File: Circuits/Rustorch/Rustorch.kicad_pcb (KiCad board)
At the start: 4 copper layers, 95 x 72 mm, 57 parts, among them CN1 USB_C_Receptacle_USB2.0_16P, CN2 OLED_128x64_IIC, Q1 2SC1815, Q2 2SC1815, Q3 2SC1815, Q4 2SC1815, SW1 ToggleSW 3P, SW2 RESET, SW3 SW_BOOT, SW4 SW_UP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

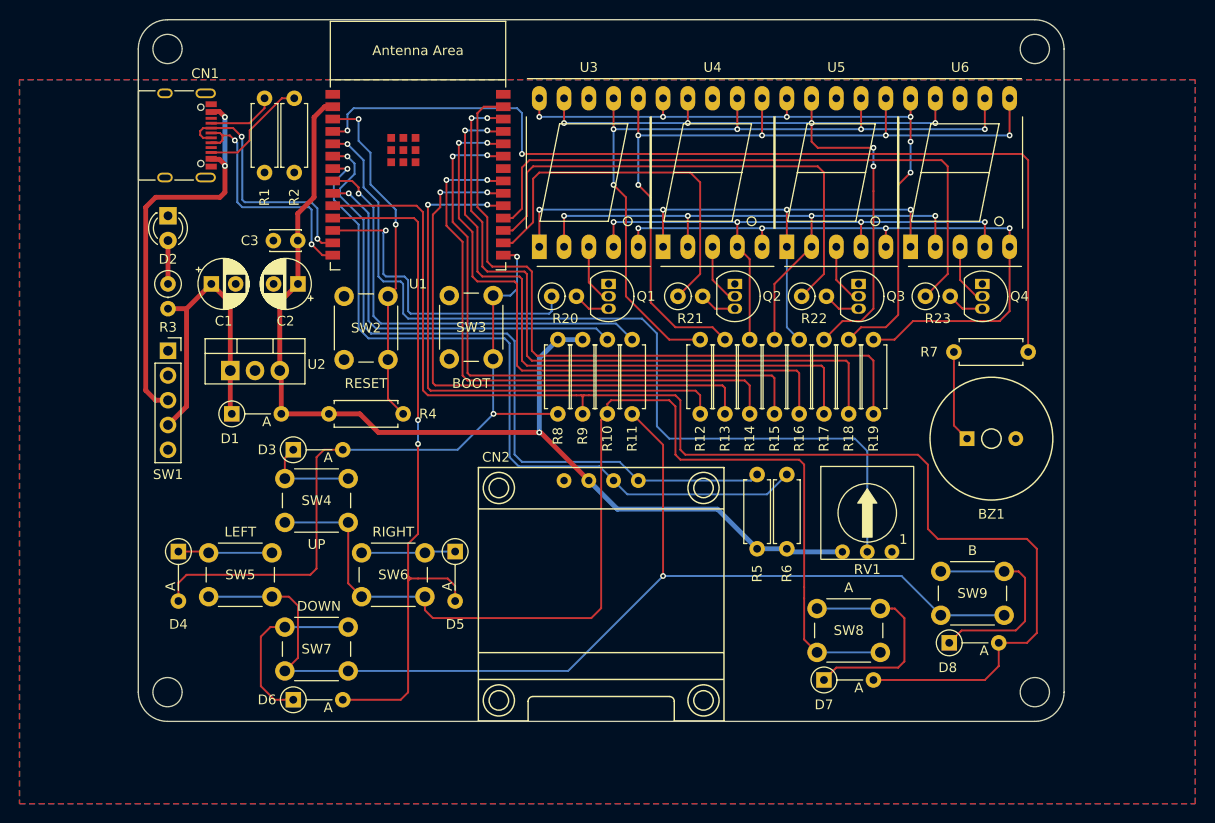
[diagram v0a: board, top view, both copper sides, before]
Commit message: (Rustorch) 配線作業 (配線を2層に削減可能な状態へ修正)
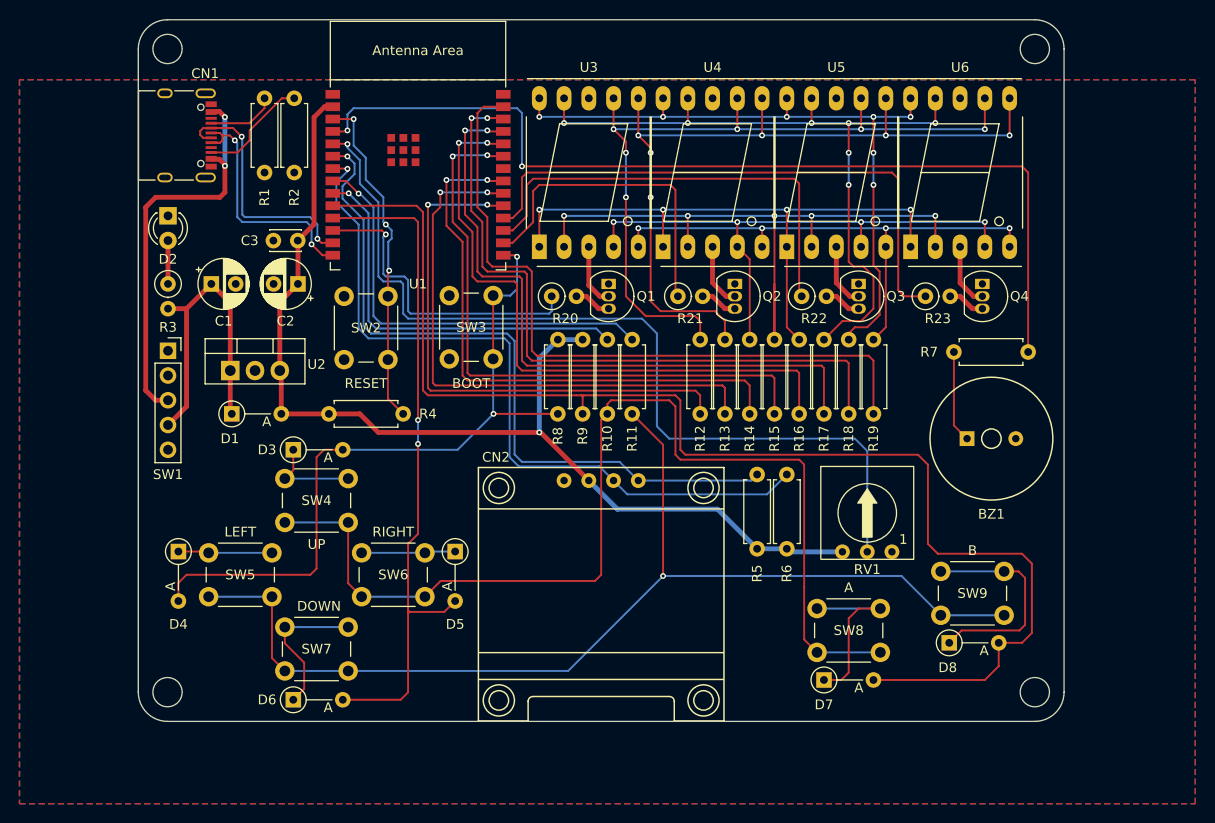
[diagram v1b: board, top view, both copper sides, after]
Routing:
- net /DP: track 67.5 -> 55.8 mm
- net /D: track 61.9 -> 69.2 mm, vias 4 -> 5
- net 7SEG_DIGIT3: track 52.2 -> 46.3 mm
- net 7SEG_DIGIT2: track 38.9 -> 33.2 mm
- net 7SEG_DIGIT4: track 65.1 -> 59.7 mm
- net Net-(R10-Pad1): track 115.0 -> 110.3 mm
- net /F: track 79.7 -> 75.4 mm, vias 6 -> 7
- net Net-(D7-K): track 22.9 -> 18.6 mm
- net Net-(D6-K): track 18.4 -> 15.2 mm
- net Net-(R11-Pad1): track 114.3 -> 112.1 mm
- net /A: track 77.9 -> 79.8 mm, vias 5 -> 6
- net /G: track 72.7 -> 70.9 mm, vias 6 -> 7
- net KEY_IN2: track 72.0 -> 70.4 mm
- net /B: track 80.2 -> 81.3 mm, vias 5 -> 6
- net KEY_IN3_IO8: track 135.3 -> 134.3 mm
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
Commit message: (Rustorch) 配線作業 (配線を2層化)
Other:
- copper layers 4 -> 2
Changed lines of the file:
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@@
 	(layers
 		(0 "F.Cu" signal)
-		(1 "In1.Cu" signal)
-		(2 "In2.Cu" signal)
 		(31 "B.Cu" signal)
 		(32 "B.Adhes" user "B.Adhesive")
@@
 			)
 			(layer "dielectric 1"
-				(type "prepreg")
-				(thickness 0.1)
-				(material "FR4")
-				(epsilon_r 4.5)
-				(loss_tangent 0.02)
-			)
-			(layer "In1.Cu"
-				(type "copper")
-				(thickness 0.035)
-			)
-			(layer "dielectric 2"
 				(type "core")
-				(thickness 1.24)
-				(material "FR4")
-				(epsilon_r 4.5)
-				(loss_tangent 0.02)
-			)
-			(layer "In2.Cu"
-				(type "copper")
-				(thickness 0.035)
-			)
-			(layer "dielectric 3"
-				(type "prepreg")
-				(thickness 0.1)
+				(thickness 1.51)
 				(material "FR4")
 				(epsilon_r 4.5)
@@
 	)
 	(segment
-		(start 116.885 85.685)
-		(end 116.865 85.665)
-		(width 0.5)
-		(layer "In2.Cu")
-		(net 4)
-	)
-	(segment
-		(start 115.175685 99.155685)
-		(end 115.02 99)
-		(width 0.5)
-		(layer "In2.Cu")
-		(net 4)
-	)
-	(segment
-		(start 141.7925 105.35)
-		(end 141.65 105.35)
-		(width 0.5)
-		(layer "In2.Cu")
-		(net 4)
-	)
-	(segment
 		(start 149.6665 113.224)
 		(end 159.938 113.224)
@@
 		(net 0)
 		(net_name "")
-		(layers "F.Cu" "In1.Cu" "In2.Cu" "B.Cu")
+		(layers "F&B.Cu")
 		(hatch edge 0.5)
 		(connect_pads

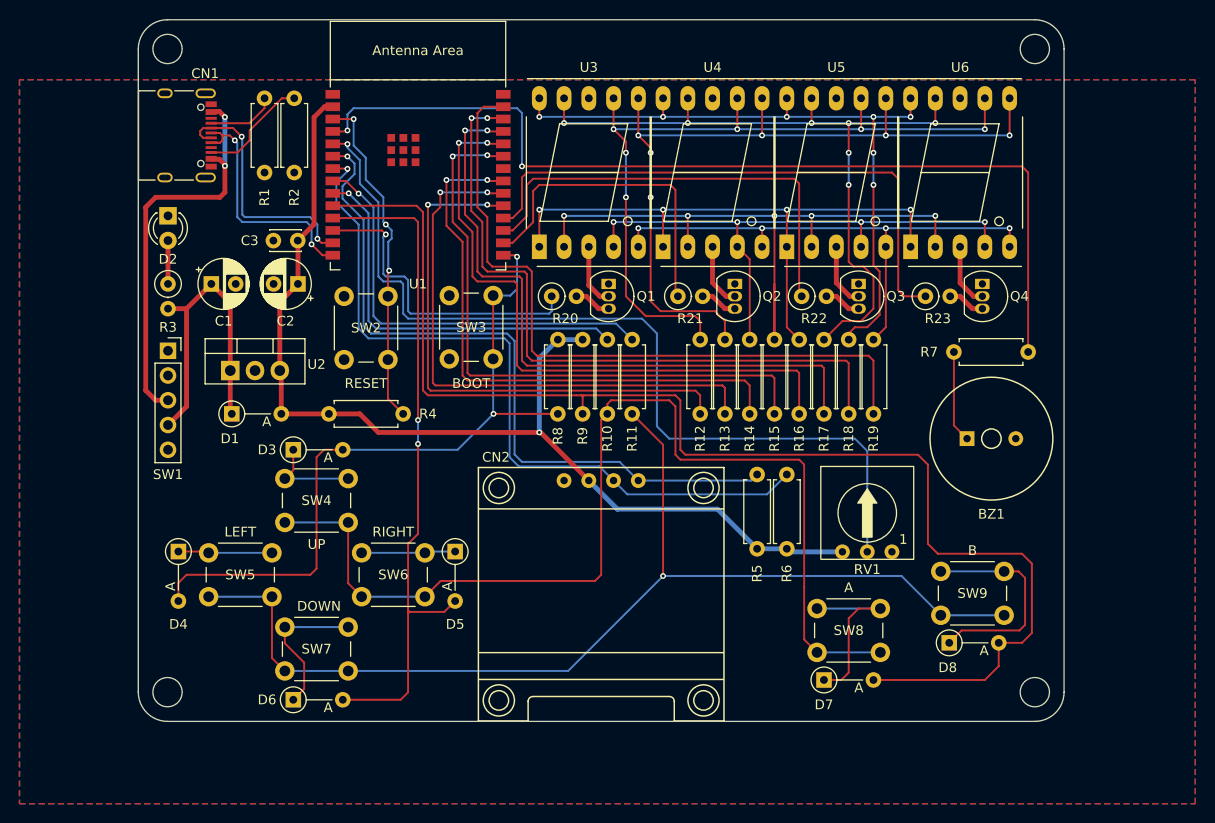
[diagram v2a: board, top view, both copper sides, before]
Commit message: (Rustorch) 配線作業 (GND ビア打ち)
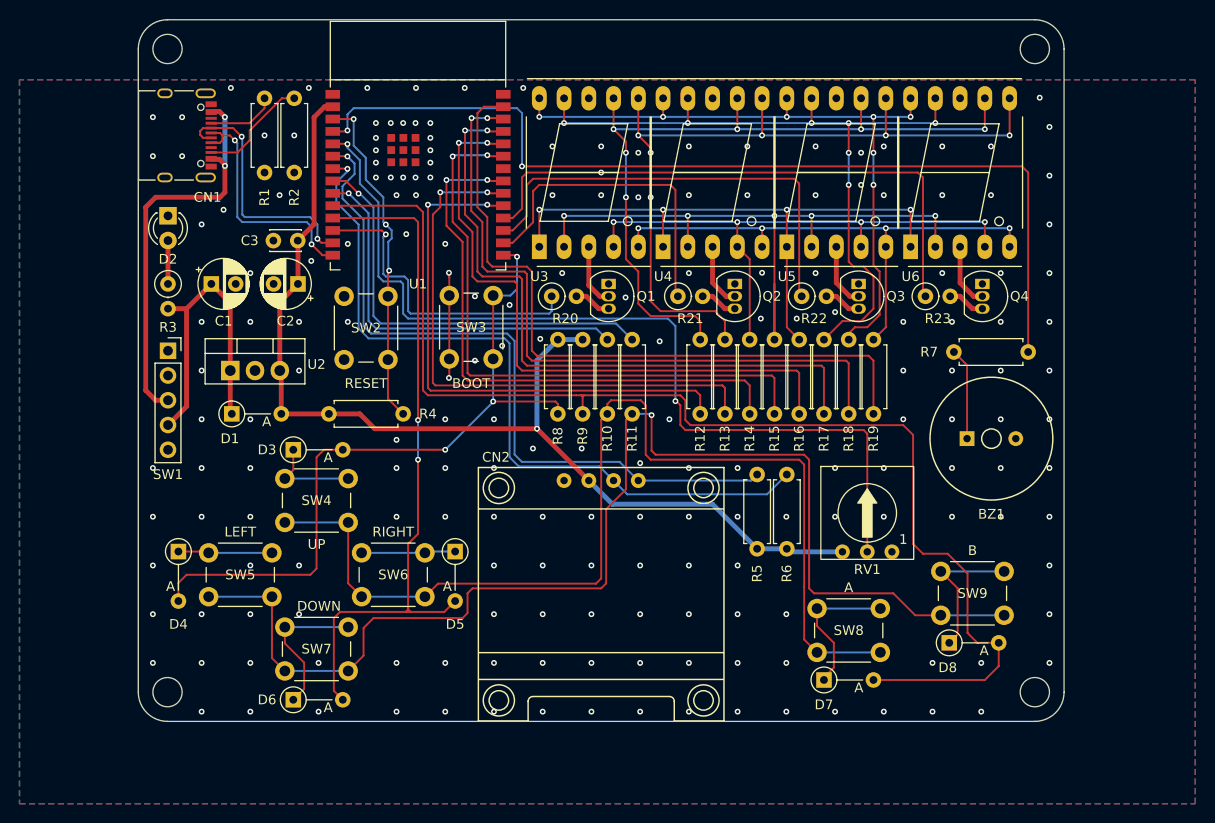
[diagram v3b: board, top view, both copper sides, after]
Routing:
- net Net-(R11-Pad1): track 112.1 -> 129.3 mm
- net GND: track 0.00 -> 10.8 mm, vias 0 -> 192
- net KEY_IN3_IO8: track 134.3 -> 126.9 mm
- net Net-(D8-K): track 22.3 -> 14.9 mm
- net Net-(D7-K): track 18.6 -> 15.0 mm
- net KEY_IN2: track 70.4 -> 72.0 mm
- net Net-(U1-MTDI/GPIO5/ADC1_CH5): track 91.7 -> 92.9 mm, vias 1 -> 2
- net 7SEG_DIGIT4: track 59.7 -> 60.0 mm, vias 0 -> 1
- net KEY_IN1_IO9_BOOT: track 75.4 -> 75.6 mm, vias 2 -> 3

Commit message: (Rustorch) 配線作業 (Teardrop 追加)
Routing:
- net 7SEG_DIGIT4: vias 1 -> 0

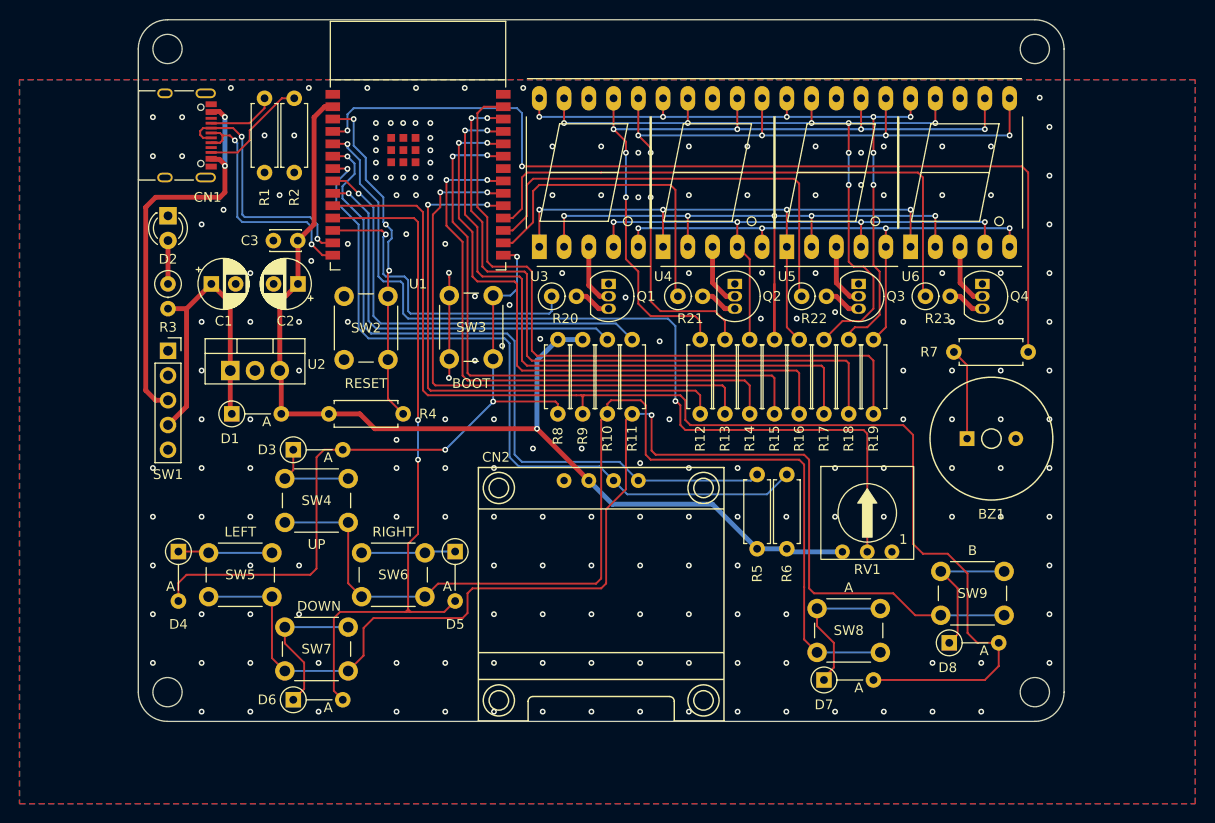
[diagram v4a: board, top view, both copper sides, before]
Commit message: (Rustorch) 配線作業 (DRC エラーの対処)
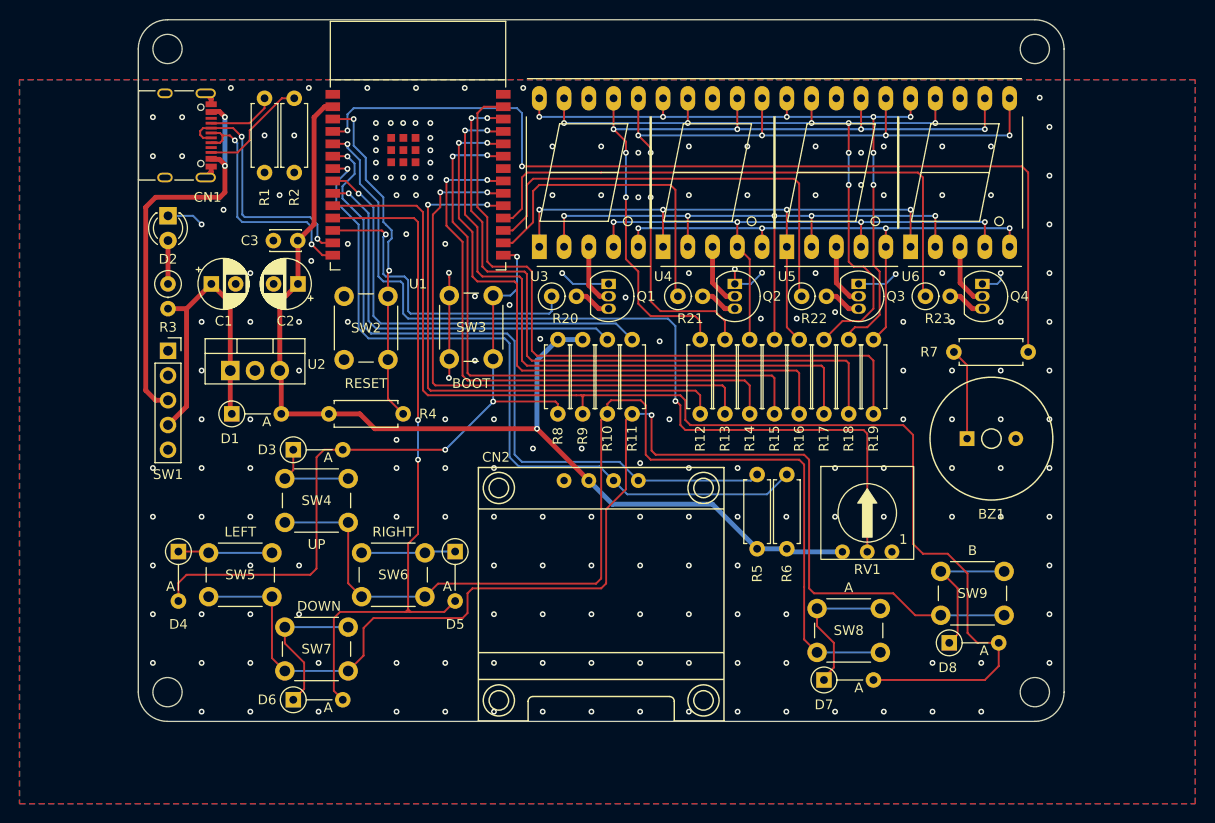
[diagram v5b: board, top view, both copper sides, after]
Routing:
- net GND: track 10.8 -> 34.4 mm, vias 192 -> 193
- net /D: track 69.2 -> 63.5 mm
- net USB_D-: track 27.8 -> 25.8 mm
- net /A: track 79.5 -> 78.8 mm
- net Net-(U1-EN/CHIP_PU): vias 3 -> 2

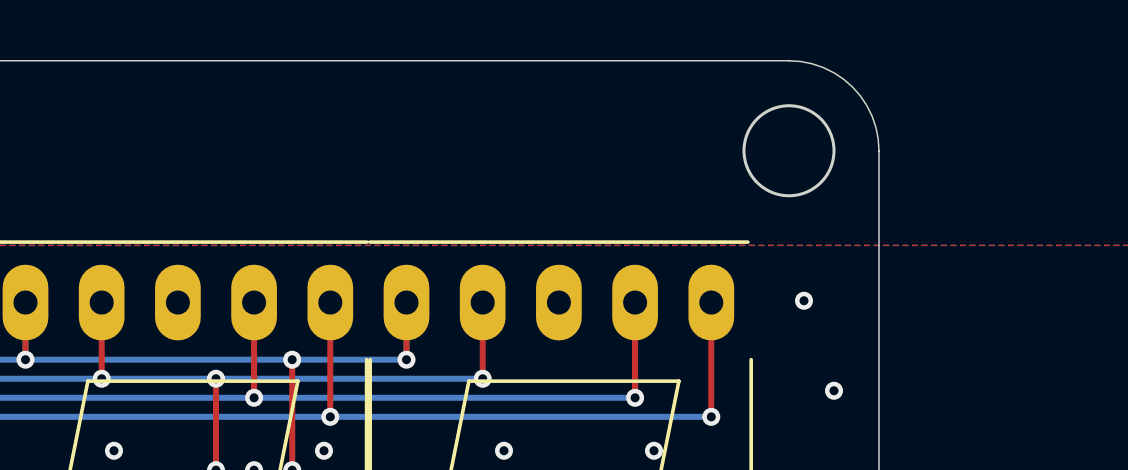
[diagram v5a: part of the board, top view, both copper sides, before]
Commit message: (Rustorch) 配線作業 (プロジェクト名・作者名のシルクを追加)
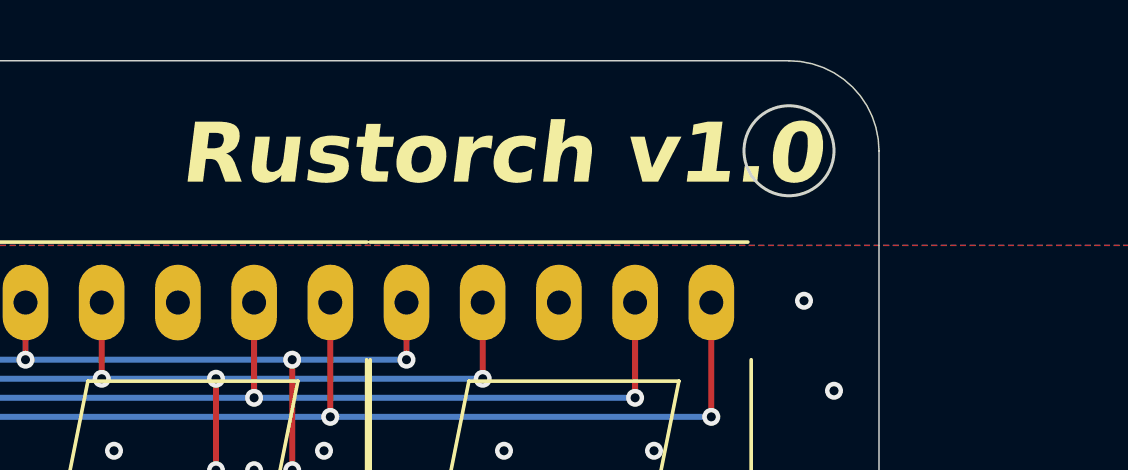
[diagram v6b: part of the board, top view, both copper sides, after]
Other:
- board text added: "@ext_sui 2024.09"
- board text added: "Rustorch v1.0"
